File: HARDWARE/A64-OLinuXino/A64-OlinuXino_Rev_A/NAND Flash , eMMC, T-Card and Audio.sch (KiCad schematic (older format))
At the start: 77 parts, among them U1 AllWinner-A64(FBGA396), U4 NA(H27UBG8T2BTR-BC(TSOP48)), U5 MTFC4GACAANA-4M_IT(TBGA100)

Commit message: A64-OLinuXino component placement, all components libraries updated
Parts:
- EMMC1: footprint (none) -> OLIMEX_Connectors-FP:GPH127SMT-02X05(PA-V16X-2X5-LF)
- EMMC_PWR1: footprint (none) -> OLIMEX_Jumpers-FP:SJ_2_SMALL
- L1: renamed from L4; footprint (none) -> OLIMEX_RLC-FP:L_0805_5MIL_DWS
- L2: renamed from L5; footprint (none) -> OLIMEX_RLC-FP:L_0805_5MIL_DWS
- L3: renamed from L1; footprint (none) -> OLIMEX_RLC-FP:L_0805_5MIL_DWS
- L4: renamed from L2; footprint (none) -> OLIMEX_RLC-FP:L_0805_5MIL_DWS
- L5: renamed from L3; footprint (none) -> OLIMEX_RLC-FP:L_0805_5MIL_DWS
- MICRO_SD1: footprint (none) -> OLIMEX_Connectors-FP:TFC-WPAPR-08
- NAND_E1: footprint (none) -> OLIMEX_Jumpers-FP:SJ
- RM1: renamed from RM3; footprint (none) -> OLIMEX_RLC-FP:RA1206_(4X0603)_4B8_xx
- RM2: renamed from RM4; footprint (none) -> OLIMEX_RLC-FP:RA0805_(4X0402)_xx
- RM3: renamed from RM5; footprint (none) -> OLIMEX_RLC-FP:RA0805_(4X0402)_xx
- RM4: renamed from RM6; footprint (none) -> OLIMEX_RLC-FP:RA1206_(4X0603)_4B8_xx
- RM5: renamed from RM7; footprint (none) -> OLIMEX_RLC-FP:RA0805_(4X0402)_xx
- RM6: renamed from RM1; footprint (none) -> OLIMEX_RLC-FP:RA0805_(4X0402)_xx
- RM7: renamed from RM8; footprint (none) -> OLIMEX_RLC-FP:RA1206_(4X0603)_4B8_xx
- RM8: renamed from RM2; footprint (none) -> OLIMEX_RLC-FP:RA1206_(4X0603)_4B8_xx
- U1: footprint (none) -> OLIMEX_IC-FP:FBGA396
- U4: footprint (none) -> OLIMEX_IC-FP:TSOP48
- U5: footprint (none) -> OLIMEX_IC-FP:TBGA100
- renumbered C41 to C34, C63 to C35, C64 to C36, C65 to C37, C66 to C38, C47 to C39, C48 to C40, C49 to C41, C59 to C42, C60 to C43, C61 to C44, C50 to C45, C34 to C46, C42 to C47, C56 to C48, C35 to C49, C43 to C50, C36 to C51, C51 to C52, C37 to C53, C44 to C54, C38 to C55, C45 to C56, C53 to C57, C57 to C58, C39 to C59, C52 to C60, C46 to C61, C58 to C62, C40 to C63, C62 to C64, C54 to C65, C55 to C66, R19 to R15, R17 to R16, R28 to R17, R29 to R18, R27 to R19, R30 to R20, R32 to R21, R18 to R22, R33 to R23, R31 to R24, R20 to R25, R25 to R26, R15 to R27, R21 to R28, R26 to R29, R34 to R30, R35 to R31, R22 to R32, R36 to R33, R23 to R34, R24 to R35, R16 to R36

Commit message: A64-OLinuXino update
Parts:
- removed unit 1 of RM5
- removed RM8: RA1206_(4x0603)_4B8_22R, OLIMEX_RLC-FP:RA1206_(4X0603)_4B8_xx, symbol RA1206_(4x0603)_4B8_Smashed
- added unit 4 of RM5
- added unit 3 of RM6
- NAND_E1: value Closed -> Soldered
- R15, R16, R17, R19, R20, R21, R22, R23, R24, R25, R26, R27, R28, R29, R30, R31, R32, R34, R35: footprint OLIMEX_RLC-FP:R_0603_5MIL_DWS -> OLIMEX_RLC-FP:R_0402_5MIL_DWS
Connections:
- net HPOUTR: now also RM6.3.1
- net NAND0-DQ4/SDC2-D4: now also RM3.4.1; no longer RM3.1.1
- net NAND0-DQ7/SDC2-D7: now also RM3.1.1; no longer RM3.4.1
- net NAND0-DQS/SDC2-RST: now also RM5.2.1; no longer RM5.3.1
- net NAND0-RB0/SDC2-CMD: now also RM5.4.1; no longer RM5.2.1
- net NAND0-RE/SDC2-CLK: now also RM5.3.1
- net at EMMC1.4, U5.P6 (CLK): now also RM5.3.2
- net at EMMC1.6, R21.1, U5.P5 (CMD): now also RM5.4.2; no longer RM5.2.2
- net at EMMC1.8, R23.1, U5.M5 (RST_N): now also RM5.2.2; no longer RM5.3.2
- net at RM3.1.2, RM4.4.2: now also U5.K9 (DAT7); no longer U5.N8 (DAT4)
- net at RM3.4.2, RM4.1.2: now also U5.N8 (DAT4); no longer U5.K9 (DAT7)
- net at C66.2: now also RM6.3.2
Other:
- moved on the sheet: RM3A, RM3D, RM4A, RM4D, RM5B, RM5C

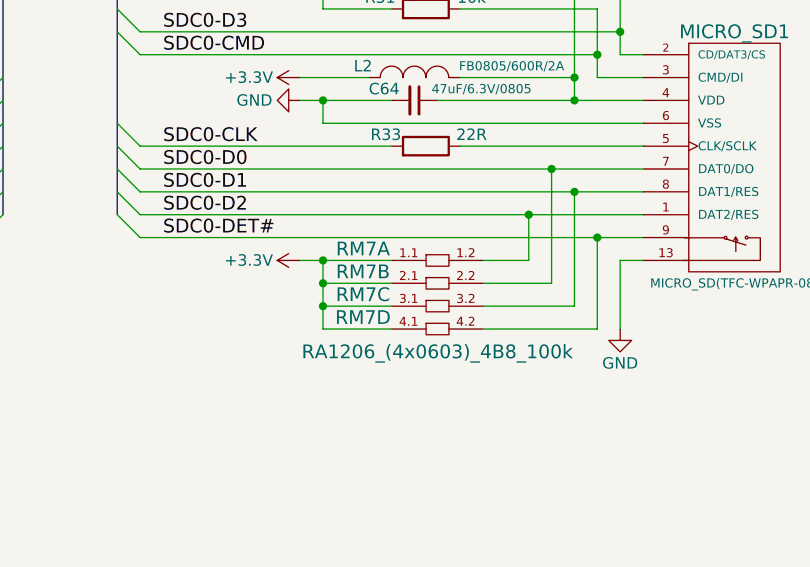
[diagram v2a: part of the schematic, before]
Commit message: A64-OLinuXino routing completed
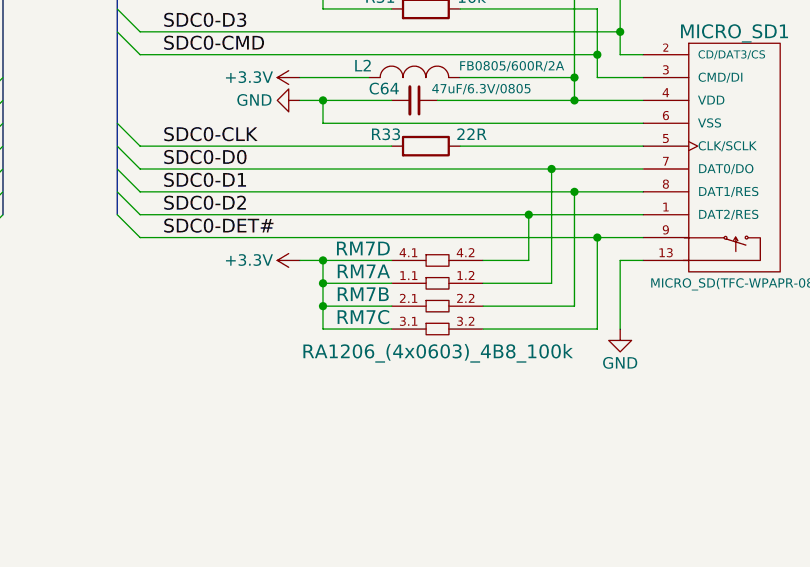
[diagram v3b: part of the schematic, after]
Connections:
- net SDC0-D0: now also RM7.1.2; no longer RM7.2.2
- net SDC0-D1: now also RM7.2.2; no longer RM7.3.2
- net SDC0-D2: now also RM7.4.2; no longer RM7.1.2
- net SDC0-DET#: now also RM7.3.2; no longer RM7.4.2
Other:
- moved on the sheet: RM7A, RM7B, RM7C, RM7D
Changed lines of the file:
@@
 EESchema Schematic File Version 2
+LIBS:OLIMEX_Antennas
+LIBS:OLIMEX_Buttons
+LIBS:OLIMEX_Connectors
+LIBS:OLIMEX_Devices
+LIBS:OLIMEX_Diodes
+LIBS:OLIMEX_IC
+LIBS:OLIMEX_Jumpers
+LIBS:OLIMEX_OTHER
+LIBS:OLIMEX_Power
+LIBS:OLIMEX_RCL
+LIBS:OLIMEX_Regulators
+LIBS:OLIMEX_Switches
+LIBS:OLIMEX_Transistors
 LIBS:A64-OlinuXino_Rev_A-cache
 EELAYER 25 0
@@
 L RA1206_(4x0603)_4B8_Smashed RM7
 U 1 1 562A4D90
-P 14100 9250
-F 0 "RM7" H 13775 9450 60  0000 C CNN
-F 1 "RA1206_(4x0603)_4B8_100k" H 14100 9000 60  0000 C CNN
-F 2 "OLIMEX_RLC-FP:RA1206_(4X0603)_4B8_xx" H 14150 9150 60  0001 C CNN
-F 3 "" H 14150 9150 60  0000 C CNN
-	1    14100 9250
+P 14100 9350
+F 0 "RM7" H 13775 9550 60  0000 C CNN
+F 1 "RA1206_(4x0603)_4B8_100k" H 14100 9200 60  0000 C CNN
+F 2 "OLIMEX_RLC-FP:RA1206_(4X0603)_4B8_xx" H 14150 9250 60  0001 C CNN
+F 3 "" H 14150 9250 60  0000 C CNN
+	1    14100 9350
 	1    0    0    -1
 $EndComp
@@
 L RA1206_(4x0603)_4B8_Smashed RM7
 U 2 1 562A4EA5
-P 14100 9350
-F 0 "RM7" H 13775 9550 60  0000 C CNN
-F 1 "RA1206_(4x0603)_4B8_100k" H 15000 9550 60  0001 C CNN
-F 2 "OLIMEX_RLC-FP:RA1206_(4X0603)_4B8_xx" H 14150 9250 60  0001 C CNN
-F 3 "" H 14150 9250 60  0000 C CNN
-	2    14100 9350
+P 14100 9450
+F 0 "RM7" H 13775 9650 60  0000 C CNN
+F 1 "RA1206_(4x0603)_4B8_100k" H 15000 9650 60  0001 C CNN
+F 2 "OLIMEX_RLC-FP:RA1206_(4X0603)_4B8_xx" H 14150 9350 60  0001 C CNN
+F 3 "" H 14150 9350 60  0000 C CNN
+	2    14100 9450
 	1    0    0    -1
 $EndComp
@@
 L RA1206_(4x0603)_4B8_Smashed RM7
 U 3 1 562A4F36
-P 14100 9450
-F 0 "RM7" H 13775 9650 60  0000 C CNN
-F 1 "RA1206_(4x0603)_4B8_100k" H 15025 9650 60  0001 C CNN
-F 2 "OLIMEX_RLC-FP:RA1206_(4X0603)_4B8_xx" H 14150 9350 60  0001 C CNN
-F 3 "" H 14150 9350 60  0000 C CNN
-	3    14100 9450
-	1    0    0    -1
-$EndComp
-$Comp
-L RA1206_(4x0603)_4B8_Smashed RM7
-U 4 1 562A4FCD
 P 14100 9550
 F 0 "RM7" H 13775 9750 60  0000 C CNN
@@
 F 2 "OLIMEX_RLC-FP:RA1206_(4X0603)_4B8_xx" H 14150 9450 60  0001 C CNN
 F 3 "" H 14150 9450 60  0000 C CNN
-	4    14100 9550
-	1    0    0    -1
-$EndComp
+	3    14100 9550
+	1    0    0    -1
+$EndComp
+$Comp
+L RA1206_(4x0603)_4B8_Smashed RM7
+U 4 1 562A4FCD
+P 14100 9250
+F 0 "RM7" H 13775 9450 60  0000 C CNN
+F 1 "RA1206_(4x0603)_4B8_100k" H 15025 9450 60  0001 C CNN
+F 2 "OLIMEX_RLC-FP:RA1206_(4X0603)_4B8_xx" H 14150 9150 60  0001 C CNN
+F 3 "" H 14150 9150 60  0000 C CNN
+	4    14100 9250
+	1    0    0    -1
+$EndComp
